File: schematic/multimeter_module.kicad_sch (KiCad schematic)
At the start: 9 parts, among them J1 Banana socket 4mm, J2 Banana socket 4mm, J3 Banana plug 4mm, J4 Banana plug 4mm, J5 Banana plug 4mm, SW1 A8L-11-11, SW2 A8L-11-11

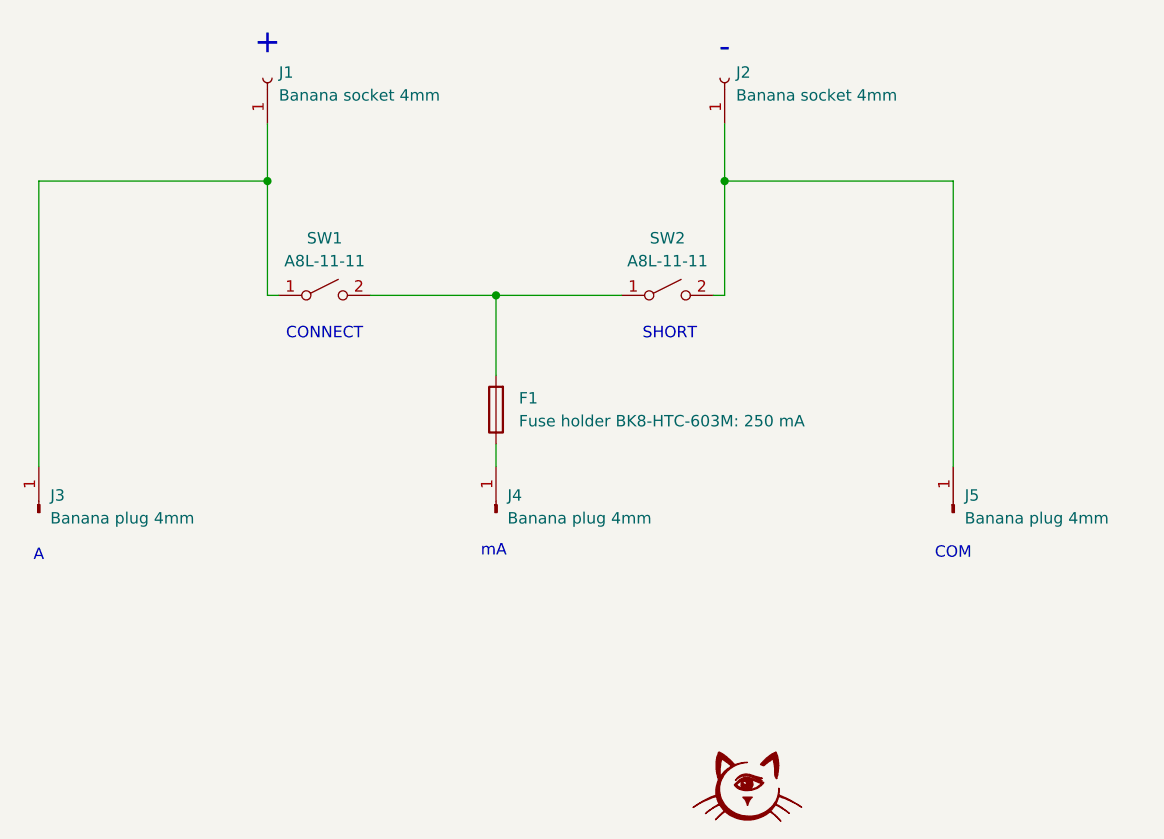
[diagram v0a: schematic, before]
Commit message: Remove 3rd plug
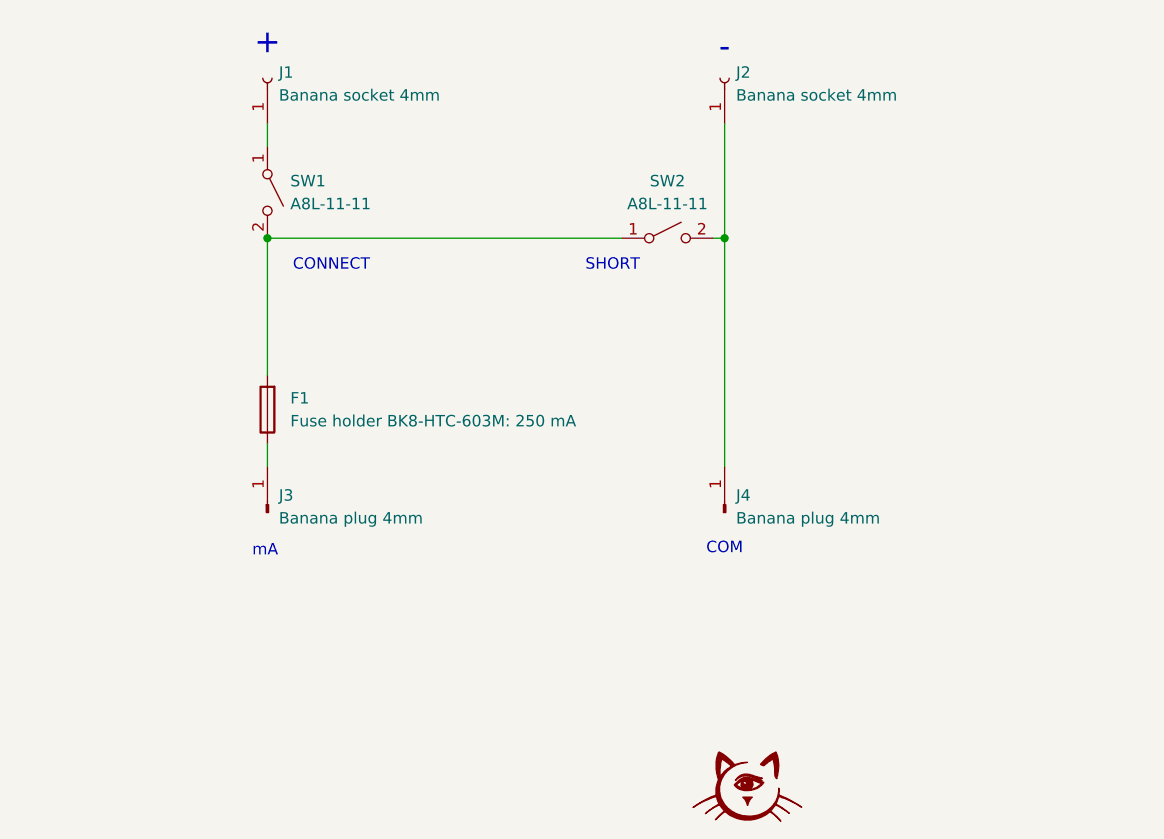
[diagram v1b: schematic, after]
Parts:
- removed J3: Banana plug 4mm, symbol Connector:Conn_01x01_Pin
- renumbered J4 to J3, J5 to J4
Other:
- note removed: "A"
- moved on the sheet: F1, J3, J4, SW1, SW2

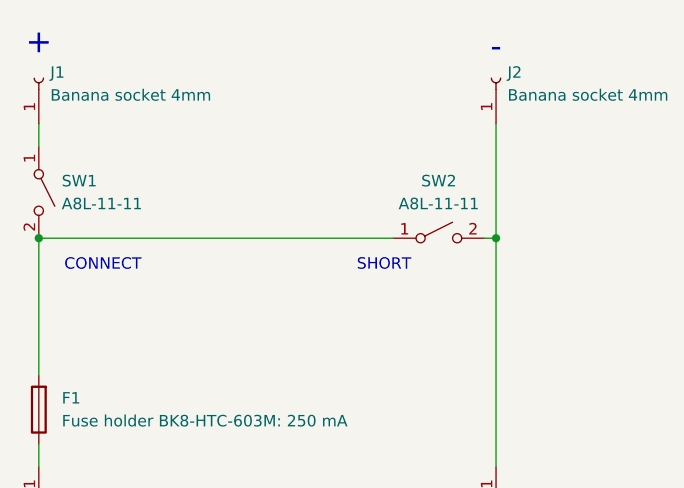
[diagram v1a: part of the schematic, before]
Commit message: Fix switch name
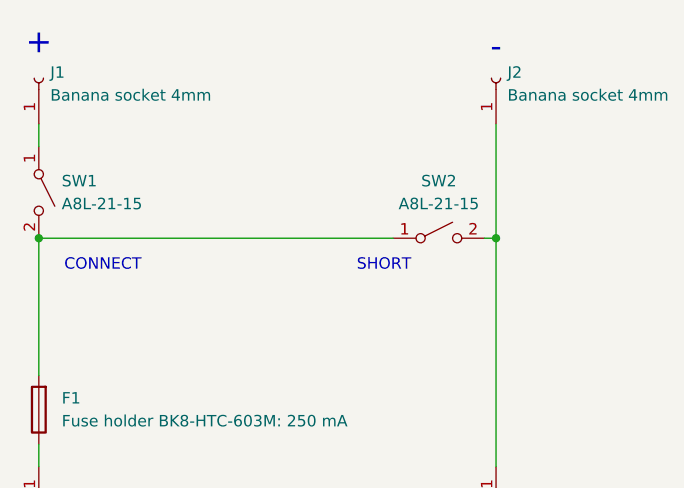
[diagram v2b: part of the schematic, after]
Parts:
- SW1, SW2: value A8L-11-11 -> A8L-21-15
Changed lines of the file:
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@@
 			)
 		)
-		(property "Value" "A8L-11-11"
+		(property "Value" "A8L-21-15"
 			(at 120.65 46.99 0)
 			(effects
@@
 			)
 		)
-		(property "Value" "A8L-11-11"
+		(property "Value" "A8L-21-15"
 			(at 78.74 46.9899 90)
 			(effects
